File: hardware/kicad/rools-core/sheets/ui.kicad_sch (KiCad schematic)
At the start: 14 parts, among them J4 ST7789, J5 J_BOT_UI, J6 J_TOP_UI, SW1 RotaryEncoder_Switch, SW2 RotaryEncoder_Switch, SW3 SW_Push

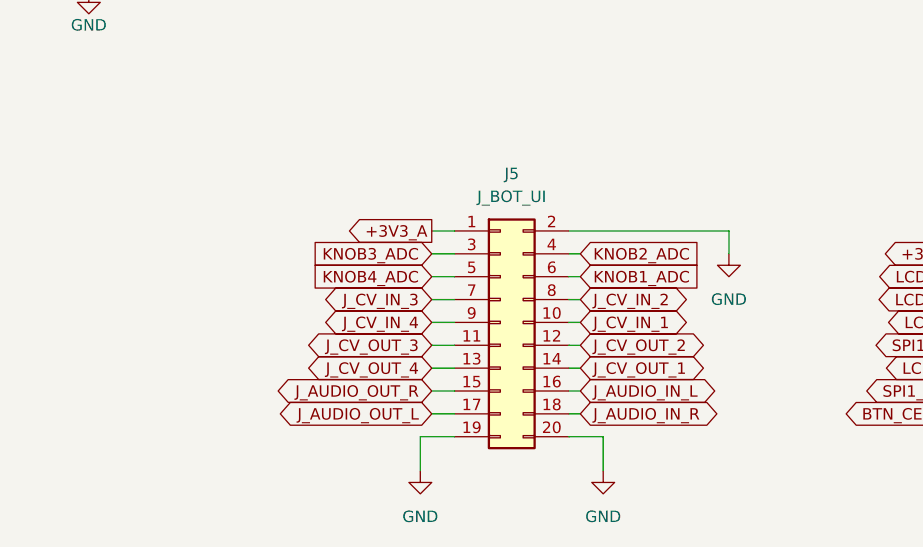
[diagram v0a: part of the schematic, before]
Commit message: Align seed schematic with Electrosmith Daisy module footprint.
Update power and UI interconnects and continue Core PCB layout after removing the local footprint library.

Co-authored-by: Cursor <cursoragent@cursor.com>
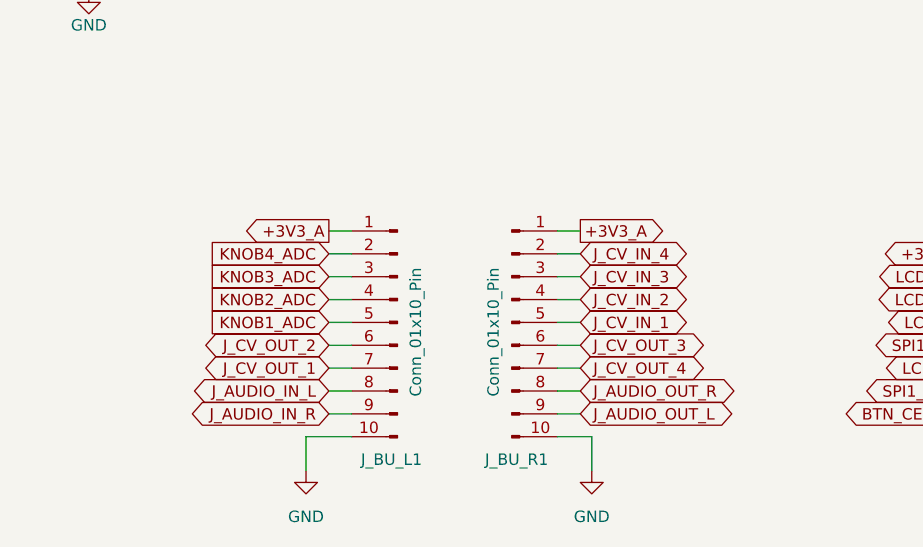
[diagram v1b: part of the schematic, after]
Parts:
- removed J5: J_BOT_UI, Connector_PinHeader_2.54mm:PinHeader_2x10_P2.54mm_Vertical_SMD, symbol Connector_Generic:Conn_02x10_Odd_Even
- added J_BU_L1, J_BU_R1: Conn_01x10_Pin, Connector_PinHeader_2.54mm:PinHeader_1x10_P2.54mm_Vertical, symbol Connector:Conn_01x10_Pin
- J6: footprint Connector_PinHeader_2.54mm:PinHeader_2x08_P2.54mm_Vertical_SMD -> Connector_PinHeader_2.54mm:PinHeader_2x08_P2.54mm_Vertical
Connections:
- net +3V3_A: now also J_BU_L1.1 (Pin_1), J_BU_R1.1 (Pin_1)
- net GND: now also J_BU_L1.10 (Pin_10), J_BU_R1.10 (Pin_10)
- net J_AUDIO_IN_L: now also J_BU_L1.8 (Pin_8)
- net J_AUDIO_IN_R: now also J_BU_L1.9 (Pin_9)
- net J_AUDIO_OUT_L: now also J_BU_R1.9 (Pin_9)
- net J_AUDIO_OUT_R: now also J_BU_R1.8 (Pin_8)
- net J_CV_IN_1: now also J_BU_R1.5 (Pin_5)
- net J_CV_IN_2: now also J_BU_R1.4 (Pin_4)
- net J_CV_IN_3: now also J_BU_R1.3 (Pin_3)
- net J_CV_IN_4: now also J_BU_R1.2 (Pin_2)
- net J_CV_OUT_1: now also J_BU_L1.7 (Pin_7)
- net J_CV_OUT_2: now also J_BU_L1.6 (Pin_6)
- net J_CV_OUT_3: now also J_BU_R1.6 (Pin_6)
- net J_CV_OUT_4: now also J_BU_R1.7 (Pin_7)
- net KNOB1_ADC: now also J_BU_L1.5 (Pin_5)
- net KNOB2_ADC: now also J_BU_L1.4 (Pin_4)
- net KNOB3_ADC: now also J_BU_L1.3 (Pin_3)
- net KNOB4_ADC: now also J_BU_L1.2 (Pin_2)
